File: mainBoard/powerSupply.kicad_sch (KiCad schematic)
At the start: 50 parts, among them J1 1366005, SW5 SW_DPST_x2, U1 MCP1727T-3302E/SN, U2 AP62250WU, U3 MCP1727T-3302E/SN

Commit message: Nearly finished with board after revisions
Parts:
- removed C1, C13, C4, C6: 10uF, Capacitor_SMD:C_0805_2012Metric_Pad1.18x1.45mm_HandSolder, symbol Device:C
- removed D4: RED, LED_SMD:LED_0603_1608Metric_Pad1.05x0.95mm_HandSolder, symbol Device:LED_Filled
- removed NT1, NT2: NetTie_2, NetTie:NetTie-2_SMD_Pad0.5mm, symbol Device:NetTie_2
- removed R1: 10k, Resistor_SMD:R_0603_1608Metric_Pad0.98x0.95mm_HandSolder, symbol Device:R_US
- removed R8: 220, Resistor_SMD:R_0603_1608Metric_Pad0.98x0.95mm_HandSolder, symbol Device:R_US
- added C1, C13, C4, C6: 10uF, Capacitor_SMD:C_Elec_6.3x5.8, symbol Device:C_Polarized
- added C39, C40: 22uF, Capacitor_SMD:C_1206_3216Metric_Pad1.33x1.80mm_HandSolder, symbol Device:C
- added D16: RED, LED_SMD:LED_0603_1608Metric_Pad1.05x0.95mm_HandSolder, symbol Device:LED_Filled
- added JP10: Jumper_2_Open, Jumper:SolderJumper-2_P1.3mm_Open_TrianglePad1.0x1.5mm, symbol Jumper:Jumper_2_Open
- added Q8, Q9: IRLML6244TRPBF, Package_TO_SOT_SMD:SOT-23, symbol Transistor_FET:IRLML6244
- added R71, R72: 10k, Resistor_SMD:R_0603_1608Metric_Pad0.98x0.95mm_HandSolder, symbol Device:R_US
- C10, C8: Type (none) -> 25V X7R
- C11, C12, C5: Type (none) -> 50V X7R
- C2, C7: footprint Capacitor_SMD:C_0805_2012Metric_Pad1.18x1.45mm_HandSolder -> Capacitor_SMD:C_0603_1608Metric_Pad1.08x0.95mm_HandSolder; Type (none) -> 50V X7R
- C3: Type (none) -> 25V Poly
- C9: Type (none) -> 35V Poly
- F1: value 1A -> 20A; footprint Fuse:Fuseholder_Clip-5x20mm_Littelfuse_100_Inline_P20.50x4.60mm_D1.30mm_Horizontal -> Fuse:Fuseholder_Clip-6.3x32mm_Littelfuse_122_Inline_P34.21x7.62mm_D2.54mm_Horizontal
- R2: value 220 -> 330
- R5: value 10k -> 330
- SW1: renamed from SW5; value SW_DPST_x2 -> SW_SPST; symbol Switch:SW_DPST_x2 -> Switch:SW_SPST
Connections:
- net LDO_SENSE_3v3 is gone; now on net LDO_VOUT_3v3: U1.7 (Sense)
- net LDO_SENSE_3v3A is gone; now on net LDO_VOUT_3v3A: U3.7 (Sense)
- net +3.3V: now also C4.1; no longer D1.2 (A)
- net +3.3VA: now also C13.1
- net +5V: now also D1.2 (A), C1.1, C39.1, C40.1, C6.1, D16.2 (A), R71.2, R72.2
- net GND: now also C1.2, C13.2, C39.2, C4.2, C40.2, C6.2, JP10.2 (B), Q8.2 (S), Q9.2 (S); no longer J1.2 (Pin_2), R2.2
- net L1_F1: now also SW1.2 (B); no longer J1.1 (Pin_1)
- net LDO_PWRGD_3v3: now also Q8.1 (G), R71.1
- net LDO_PWRGD_3v3A: now also Q9.1 (G), R72.1; no longer R5.2
- net LDO_VOUT_3v3A: no longer R5.1
- net L1 renamed L1_SW
- net L1_SW: now also PS1.2 (AC/L); no longer F1.2
- removed net L1_F1_SW: PS1.2 (AC/L), SW1.2 (B)
- new net: Q9.3 (D), R5.2
- new net: Q8.3 (D), R2.2
- new net 3VA3_K: D16.1 (K), R5.1
- new net GNDPWR: J1.2 (Pin_2), JP10.1 (A)
- new net L1-120VAC: F1.2, J1.1 (Pin_1)
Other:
- note added: "120VAC - 12VDC Supply"
- note added: "3.3VDC LDO Analog"
- note added: "3.3VDC LDO Digital"
- note added: "5VDC Buck Converter"
- note removed: "52000001009"
- note removed: "CL21A106KQFNNNE"
- note removed: "CL21B105KAFNNNE"
- note removed: "CL31A226MOCLNNC x2"
- moved on the sheet: C10, C11, C12, C2, C3, C5, C8, C9, D1, D2, D3, H1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

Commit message: work on AC power side
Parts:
- added C41: 47nF, Capacitor_SMD:C_0603_1608Metric_Pad1.08x0.95mm_HandSolder, symbol Device:C
- added C42: 100nF, Capacitor_SMD:C_0603_1608Metric_Pad1.08x0.95mm_HandSolder, symbol Device:C
- added C43: 100nF, Capacitor_THT:C_Rect_L18.0mm_W5.0mm_P15.00mm_FKS3_FKP3, symbol Device:C
- added R73: 1M, Resistor_SMD:R_2512_6332Metric_Pad1.40x3.35mm_HandSolder, symbol Device:R_US
- C1, C13, C4, C6: value 10uF -> 22uF; Type 25V Poly -> 16V Poly; part number (none) -> A768EB226M1HLAE048
- C10, C8: Type 25V X7R -> 50V X7R
- C2, C7: value 100nF -> 47nF; Type 50V X7R -> 16V C0G
- C39, C40: Type 25V X7R -> 50V X7R; now not fitted
- H1: footprint MountingHole:MountingHole_2.7mm -> MountingHole:MountingHole_2.7mm_Pad_Via
- H2, H3, H4, H5, H6: symbol Mechanical:MountingHole_Pad -> Mechanical:MountingHole
- J1: footprint PhoenixContact_SPTA:SPTA-THR 2.53-5.0 P26 -> PhoenixContact_1714984:CONN_1714984_PXC
- R3: value 52.3k -> 52.3k 1%
- R4: value 10k -> 10k 1%
- SW1: footprint TerminalBlock_Phoenix:TerminalBlock_Phoenix_MKDS-1,5-2-5.08_1x02_P5.08mm_Horizontal -> PhoenixContact_MKDS_9mm:CONN_1714971_PXC
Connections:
- net +12V: now also C42.1; no longer C11.1, C12.1, C9.1
- net AC_DC_+12V: now also C11.1, C12.1, C9.1
- net GND: now also C41.2, C42.2
- net GNDPWR: now also H1.1
- net L1_SW: now also C43.1, R73.2
- net LN: now also C43.2, R73.1
- net 5V_BUCK_EN: now reaches U2.5 (EN)
- net 5V_BUCK_EN: now also C41.1
- net 5V_BUCK_BST renamed +5V_BUCK_BST
- net 5V_BUCK_FB renamed +5V_BUCK_FB
- net 5V_BUCK_SW renamed +5V_BUCK_SW
- net 5V_BUCK_VOUT renamed +5V_BUCK_VOUT
- net LDO_VOUT_3v3 renamed LDO_VOUT_+3v3
- net LDO_VOUT_3v3A renamed LDO_VOUT_+3v3A
- no-connect marks 7 -> 0
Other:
- note removed: "A765KG106M1ELAE035"
- note removed: "A768EB476M1VLAE042"
- note removed: "MAMK2520T2R2M"
- moved on the sheet: C10, C11, C12, C3, C5, C8, C9, D2, D3, F1, J1, JP10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

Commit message: still arranging AC side
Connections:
- net L1_F1: now also SW1.1 (A); no longer SW1.2 (B)
- net L1_SW: now also SW1.2 (B); no longer SW1.1 (A)
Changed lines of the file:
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@@
 		(lib_id "Switch:SW_SPST")
 		(at 151.13 66.04 0)
-		(mirror y)
 		(unit 1)
 		(body_style 1)

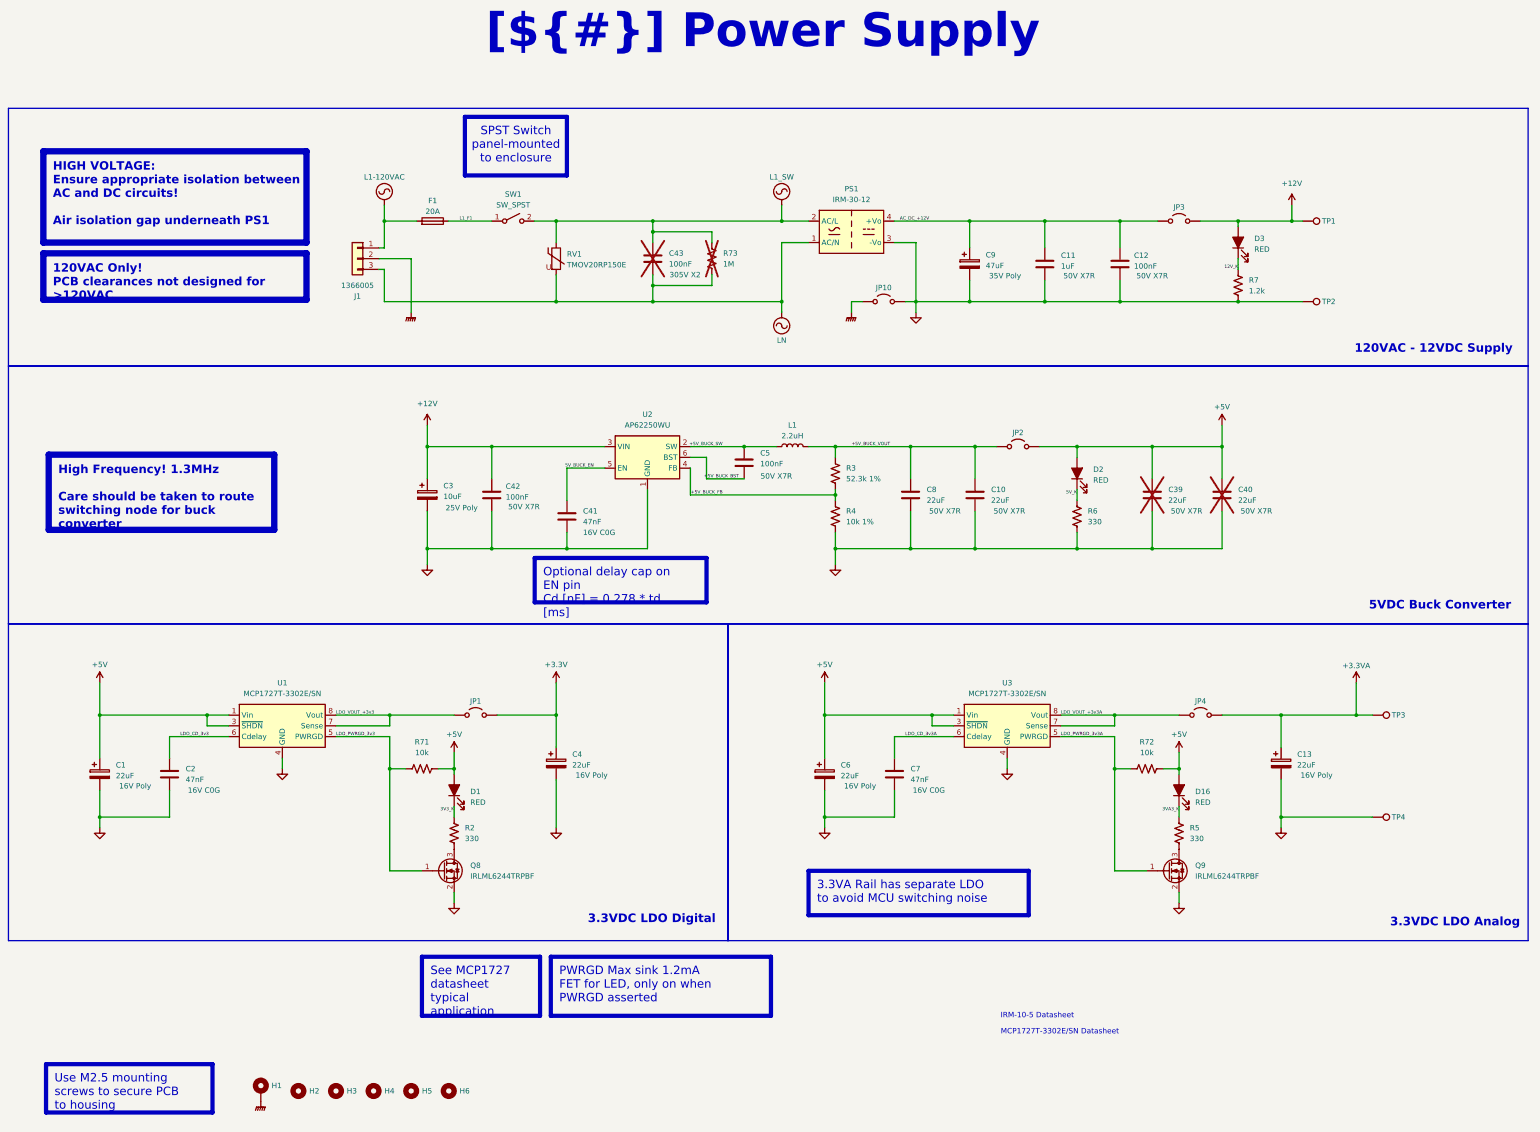
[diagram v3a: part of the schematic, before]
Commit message: add USB-A and change capacitors
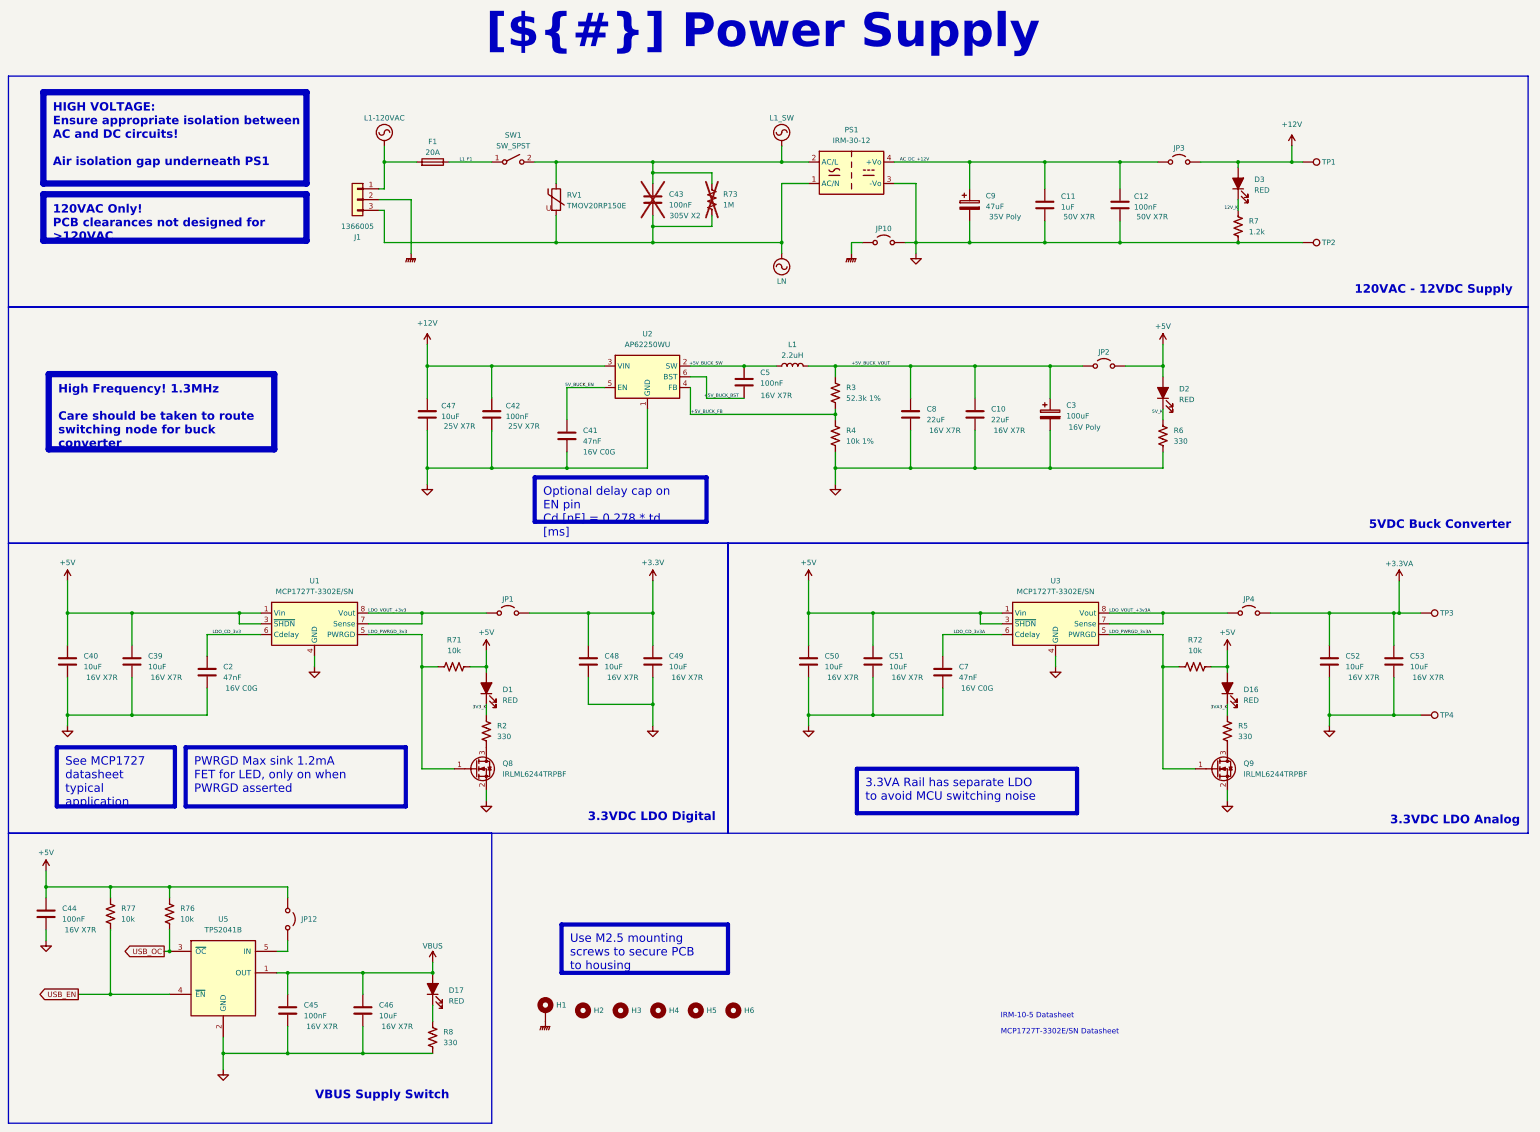
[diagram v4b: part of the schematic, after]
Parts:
- removed C1, C13, C4, C6: 22uF, Capacitor_SMD:C_Elec_6.3x5.8, symbol Device:C_Polarized
- added C44, C45: 100nF, Capacitor_SMD:C_0603_1608Metric_Pad1.08x0.95mm_HandSolder, symbol Device:C
- added C46: 10uF, Capacitor_SMD:C_0603_1608Metric_Pad1.08x0.95mm_HandSolder, symbol Device:C
- added C47: 10uF, Capacitor_SMD:C_1206_3216Metric_Pad1.33x1.80mm_HandSolder, symbol Device:C
- added C48, C49, C50, C51, C52, C53: 10uF, Capacitor_SMD:C_0805_2012Metric_Pad1.18x1.45mm_HandSolder, symbol Device:C
- added D17: RED, LED_SMD:LED_0603_1608Metric_Pad1.05x0.95mm_HandSolder, symbol Device:LED_Filled
- added JP12: Jumper_2_Open, Connector_PinHeader_2.54mm:PinHeader_1x02_P2.54mm_Vertical, symbol Jumper:Jumper_2_Open
- added R76, R77: 10k, Resistor_SMD:R_0603_1608Metric_Pad0.98x0.95mm_HandSolder, symbol Device:R_US
- added R8: 330, Resistor_SMD:R_0603_1608Metric_Pad0.98x0.95mm_HandSolder, symbol Device:R_US
- added U5: TPS2041B, Package_TO_SOT_SMD:SOT-23-5, symbol Power_Management:TPS2041B
- C10, C5, C8: Type 50V X7R -> 16V X7R
- C3: value 10uF -> 100uF; Type 25V Poly -> 16V Poly
- C39, C40: value 22uF -> 10uF; footprint Capacitor_SMD:C_1206_3216Metric_Pad1.33x1.80mm_HandSolder -> Capacitor_SMD:C_0805_2012Metric_Pad1.18x1.45mm_HandSolder; Type 50V X7R -> 16V X7R; now fitted
- C42: Type 50V X7R -> 25V X7R
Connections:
- net +12V: now also C47.1; no longer C3.1
- net +3.3V: now also C48.1, C49.1
- net +3.3VA: now also C52.1, C53.1
- net +5V: now also C44.1, C50.1, C51.1, JP12.1 (A), R76.2, R77.2
- net +5V_BUCK_VOUT: now also C3.1
- net GND: now also C44.2, C45.2, C46.2, C47.2, C48.2, C49.2, C50.2, C51.2, C52.2, C53.2, R8.2, U5.2 (GND)
- new net: D17.1 (K), R8.1
- new net: JP12.2 (B), U5.5 (IN)
- new net USB_EN: R77.1, U5.4 (~{EN})
- new net USB_OC: R76.1, U5.3 (~{OC})
- new net VBUS: C45.1, C46.1, D17.2 (A), U5.1 (OUT)
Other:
- note added: "VBUS Supply Switch"
- moved on the sheet: C10, C11, C12, C2, C3, C41, C42, C43, C5, C7, C8, C9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
